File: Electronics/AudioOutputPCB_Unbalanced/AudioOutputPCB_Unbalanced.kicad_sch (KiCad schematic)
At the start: 93 parts, among them J1 IDC, J2 RCA x2, J3 RCA x2, J4 RCA x2, J5 RCA x2, U1 NE5532, U2 NE5532, U3 NE5532, U4 NE5532

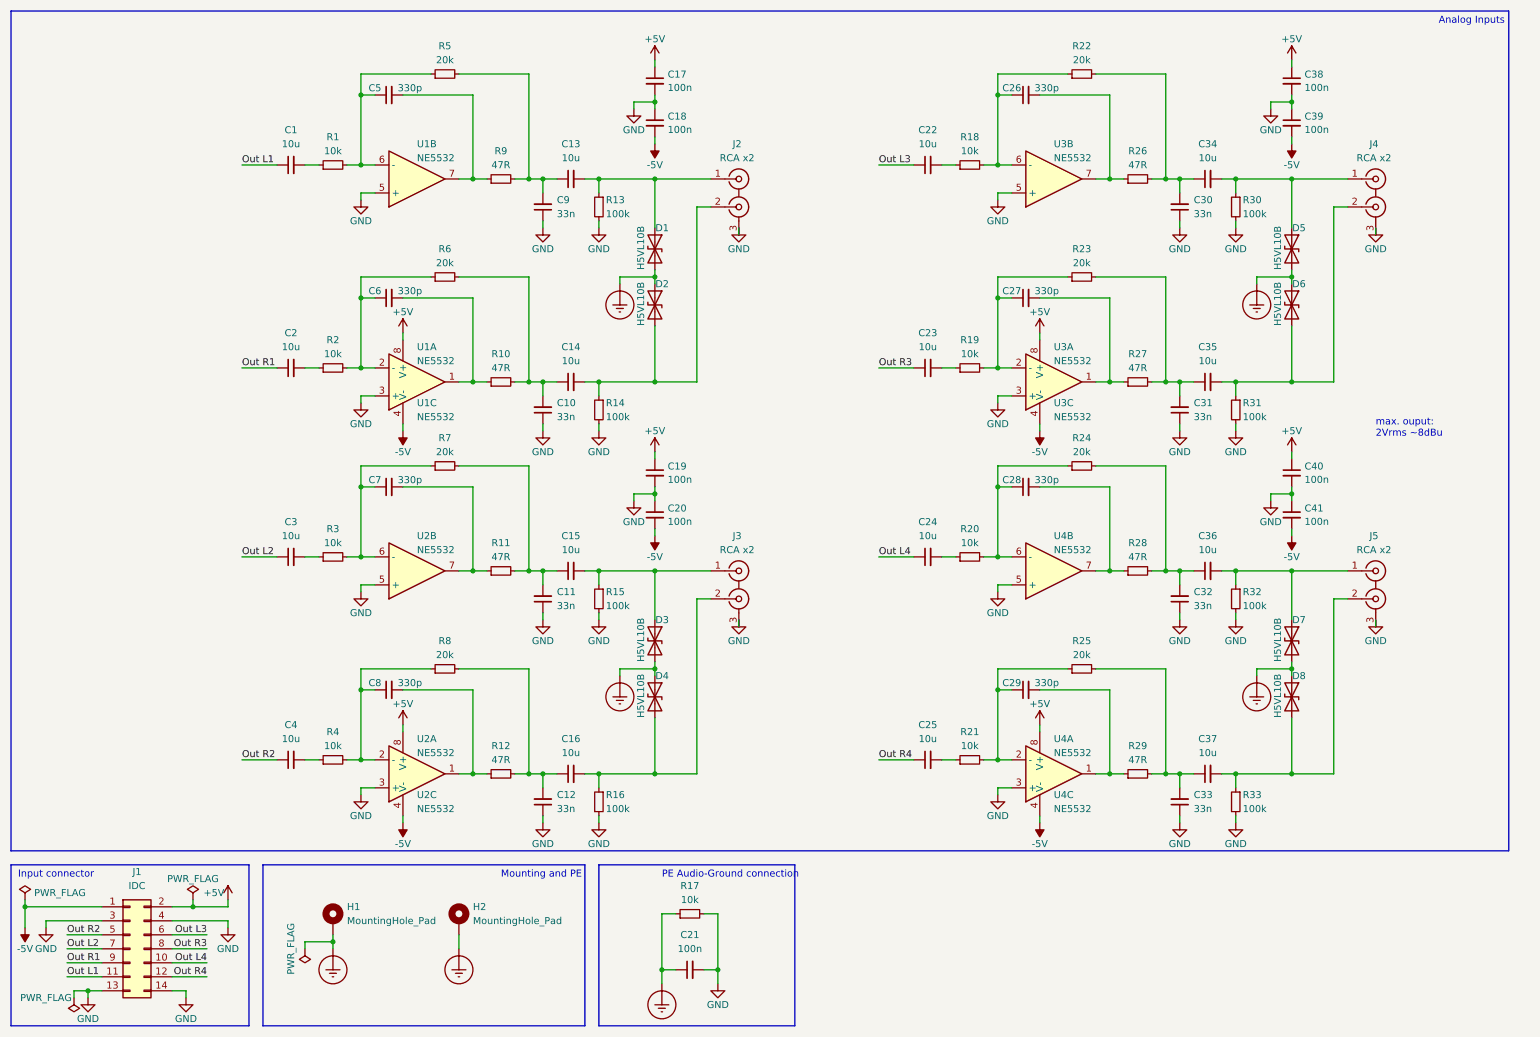
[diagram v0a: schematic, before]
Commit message: Final commit before fabrication of: Maxi, Unbal In and Unbal Out Rev1.0
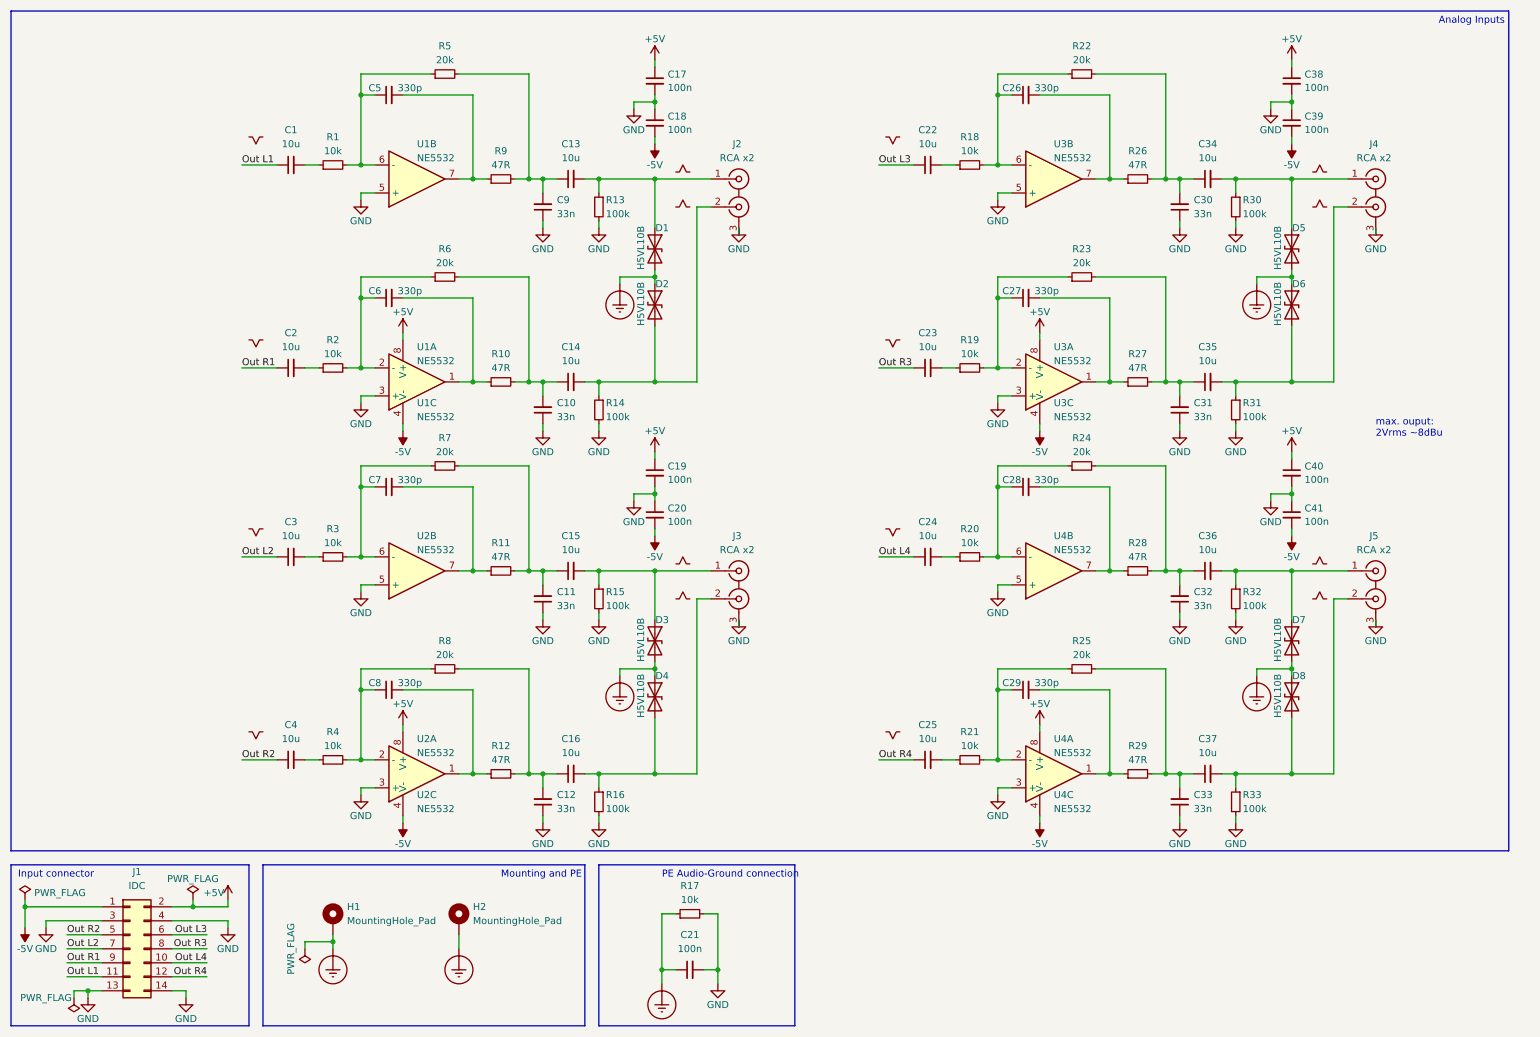
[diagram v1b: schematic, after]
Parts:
- added S1, S10, S11, S12, S13, S14, S15, S16, S2, S3, S4, S5, S6, S7, S8, S9: Phase, symbol 1_Project_Symbols:Phase
